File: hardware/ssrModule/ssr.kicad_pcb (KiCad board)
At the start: 2 copper layers, 112 x 90 mm, 113 parts, among them J1 Button-Sensors-MicroMatch2X03, J12 RJ45-CAN, J13 WAGO2604-1102, J2 WAGO2604-1108, J3 WAGO2604-1108, J5 IRDA, J6 IRDA, J7 RJ45-CAN, Q1 BC847, Q2 BC847, U1 PESD2CAN, U10 AQH3213A, U11 AQH3213A, U12 AQH3213A, U13 AQH3213A, U14 AQH3213A, U15 AQH3213A, U16 AQH3213A, U17 AQH3213A, U18 AQH3213A, U19 AQH3213A, U2 MCP2562-E-SN, U20 AQH3213A, U21 AQH3213A, U22 AQH3213A, U23 AQH3213A, U3 ESP32-WROOM-32, U4 MCP1703A-3302_SOT89, U5 PCF8574A, U6 PCF8574A, U7 AQH3213A, U8 AQH3213A, U9 wuerthDebug6

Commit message: feat: Add second fuse for ssr
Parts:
- added F2: 1A sehr träge, Fuse:Fuseholder_Cylinder-5x20mm_Schurter_0031_8201_Horizontal_Open, F.Cu at (78.0, 83.2)
- moved U12 5.71 mm to (90.2, 83.5)
- moved U18 5.71 mm to (90.2, 94.0)
- moved U13 5.71 mm to (104.0, 81.0)
- moved U19 5.71 mm to (104.0, 91.5)
- moved U20 5.71 mm to (104.0, 102.0)
- moved U21 5.71 mm to (119.7, 102.0)
- moved U22 5.71 mm to (119.7, 91.5)
- moved U23 5.71 mm to (119.7, 81.0)
- moved U10 5.50 mm to (40.5, 91.0)
- moved U11 5.50 mm to (53.8, 83.2)
- moved U14 5.50 mm to (24.0, 91.0)
- moved U15 5.50 mm to (40.5, 101.5)
- moved U16 5.50 mm to (40.5, 80.5)
- moved U17 5.50 mm to (53.8, 93.8)
- moved U7 5.50 mm to (24.0, 80.5)
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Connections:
- F1 pad 1: AC -> /AC1
- U10 pad 8: AC -> /AC1
- U11 pad 8: AC -> /AC1
- U12 pad 8: AC -> /AC2
- U13 pad 8: AC -> /AC2
- U14 pad 8: AC -> /AC1
- U15 pad 8: AC -> /AC1
- U16 pad 8: AC -> /AC1
- U17 pad 8: AC -> /AC1
- U18 pad 8: AC -> /AC2
- U19 pad 8: AC -> /AC2
- U20 pad 8: AC -> /AC2
- U21 pad 8: AC -> /AC2
- U22 pad 8: AC -> /AC2
- U23 pad 8: AC -> /AC2
- U7 pad 8: AC -> /AC1
- U8 pad 8: AC -> /AC1
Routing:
- net AC: track 243.6 -> 0.00 mm
- net /AC1: track 0.00 -> 125.9 mm
- net /AC2: track 0.00 -> 116.9 mm
- net Net-(F1-Pad2): track 66.0 -> 84.6 mm
- net GND: track 215.1 -> 232.1 mm, vias 12 -> 16
- net /OUTPUT11: track 54.4 -> 63.9 mm
- net /OUTPUT6: track 55.8 -> 64.4 mm
- net /OUTPUT5: track 42.9 -> 51.1 mm
- net /OUTPUT12: track 40.9 -> 47.9 mm
- net Net-(R36-Pad2): track 27.6 -> 21.8 mm, vias 2 -> 0
- net /OUTPUT13: track 27.4 -> 33.1 mm
- net Net-(R22-Pad2): track 18.7 -> 24.3 mm
- net Net-(R31-Pad2): track 27.9 -> 33.5 mm
- net /OUTPUT7: track 52.0 -> 47.1 mm
- net Net-(R20-Pad2): track 13.1 -> 17.7 mm
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
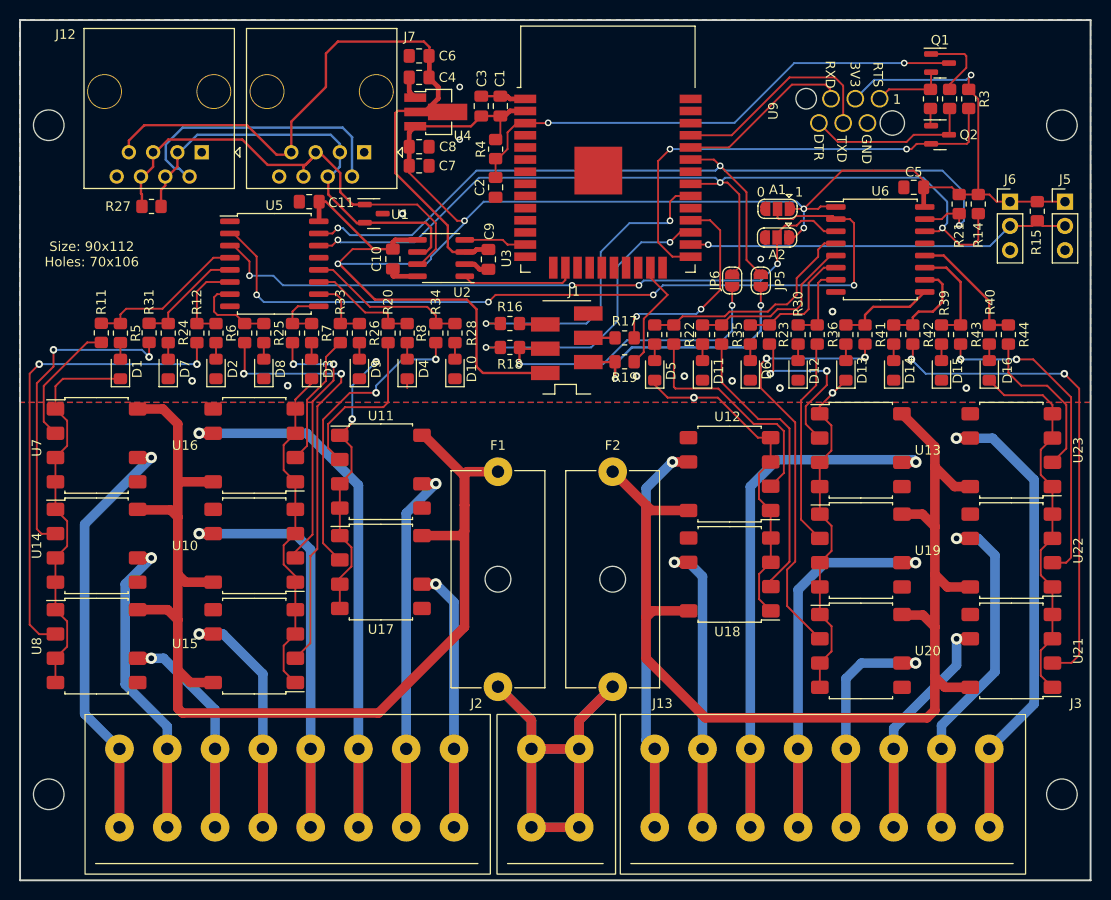
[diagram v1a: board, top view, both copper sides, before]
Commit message: feat: change PCB debug to EN/BOOT0
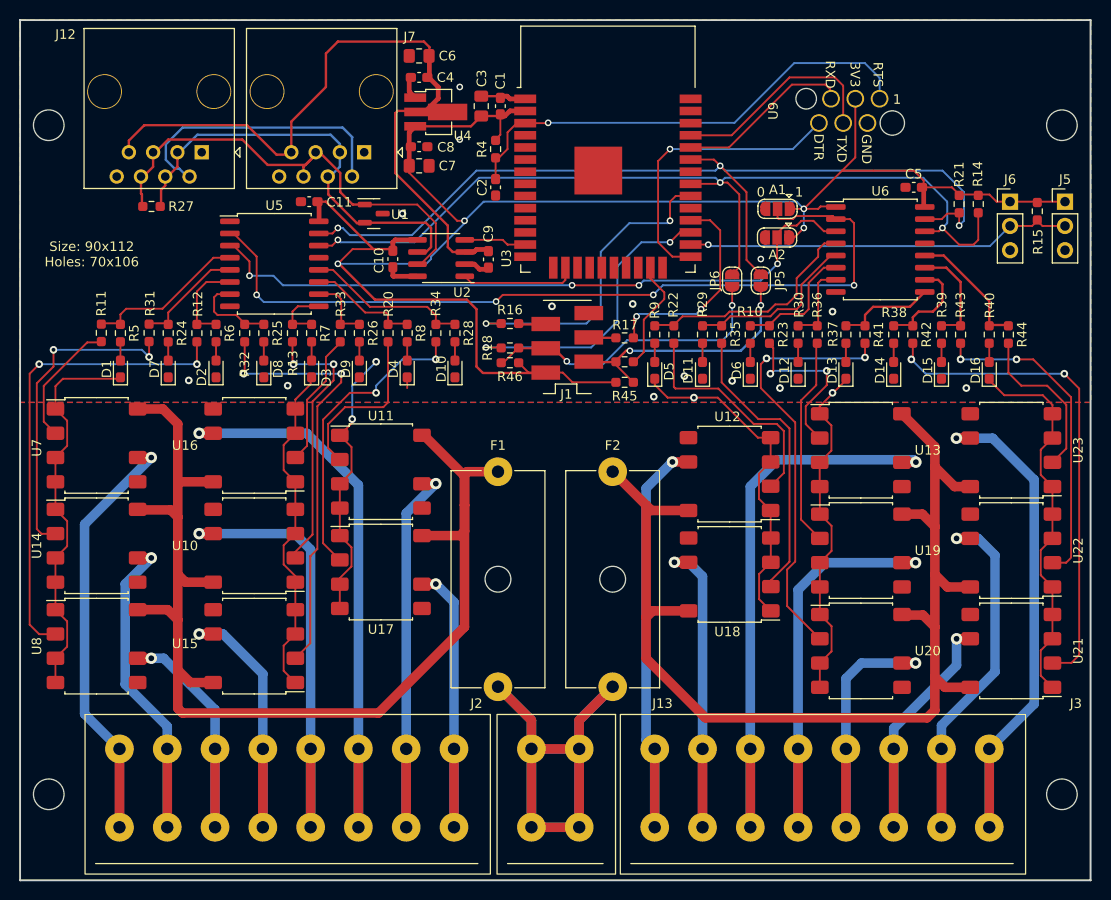
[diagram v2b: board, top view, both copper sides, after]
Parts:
- removed Q1, Q2: BC847, Package_TO_SOT_SMD:SOT-23
- removed R1, R2, R3: 10K, Resistor_SMD:R_0805_2012Metric_Pad1.20x1.40mm_HandSolder
- added R45: 2K2, Resistor_SMD:R_0603_1608Metric_Pad0.98x0.95mm_HandSolder, F.Cu at (79.2, 73.9)
- added R46: 2K2, Resistor_SMD:R_0603_1608Metric_Pad0.98x0.95mm_HandSolder, F.Cu at (67.2, 71.8)
- C1, C10, C11, C2, C4, C5, C8, C9: footprint Capacitor_SMD:C_0805_2012Metric_Pad1.18x1.45mm_HandSolder -> Capacitor_SMD:C_0603_1608Metric_Pad1.08x0.95mm_HandSolder
- D1, D10, D11, D12, D13, D14, D15, D16, D2, D3, D4, D5, D6, D7, D8, D9: footprint LED_SMD:LED_0805_2012Metric_Pad1.15x1.40mm_HandSolder -> LED_SMD:LED_0603_1608Metric_Pad1.05x0.95mm_HandSolder
- R10, R11, R12, R13, R14, R15, R16, R17, R18, R19, R20, R21, R22, R23, R24, R25, R26, R27, R28, R29, R30, R31, R32, R33, R34, R35, R36, R37, R38, R39, R4, R40, R41, R42, R43, R44, R5, R6, R7, R8, R9: footprint Resistor_SMD:R_0805_2012Metric_Pad1.20x1.40mm_HandSolder -> Resistor_SMD:R_0603_1608Metric_Pad0.98x0.95mm_HandSolder
- moved J1 5.97 mm to (73.2, 69.8), turned to 180 degrees
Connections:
- J1 pad 1: GND -> +3V3
- J1 pad 2: Net-(J1-Pad2) -> /SDA_EXT
- J1 pad 3: Net-(J1-Pad3) -> /SCL_EXT
- J1 pad 4: /SCL_EXT -> Net-(J1-Pad4)
- J1 pad 5: /SDA_EXT -> Net-(J1-Pad5)
- J1 pad 6: +3V3 -> GND
- R16 pad 2: Net-(J1-Pad2) -> Net-(J1-Pad5)
- R17 pad 2: Net-(J1-Pad3) -> Net-(J1-Pad4)
- U9 pad 1: /RTS -> /EN
- U9 pad 6: /DTR -> /BOOT0
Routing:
- net /BOOT0: track 49.4 -> 31.0 mm, vias 2 -> 1
- net /DTR: track 17.5 -> 0.00 mm
- net Net-(Q1-Pad1): track 8.00 -> 0.00 mm
- net /RTS: track 7.56 -> 0.00 mm
- net +3V3: track 197.3 -> 190.2 mm, vias 5 -> 4
- net /EN: track 54.6 -> 50.1 mm, vias 2 -> 1
- net Net-(J1-Pad4): track 0.00 -> 2.80 mm
- net Net-(J1-Pad3): track 2.80 -> 0.00 mm
- net Net-(J1-Pad5): track 0.00 -> 2.74 mm
- net Net-(J1-Pad2): track 2.74 -> 0.00 mm
- net Net-(Q2-Pad1): track 1.83 -> 0.00 mm
- net /SCL_EXT: track 32.8 -> 31.6 mm
- net GND: vias 16 -> 18
